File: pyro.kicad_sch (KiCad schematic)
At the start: 6 parts, among them J14 PYRO, Q1 CSD17571Q2

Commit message: replaced signal blocks, shortening board, adding precise positioning
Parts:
- renumbered J14 to J15, Q1 to Q2, R51 to R52, R52 to R53, R53 to R54
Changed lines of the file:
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@@
 		(dnp no)
 		(fields_autoplaced yes)
-		(property "Reference" "#PWR0108"
+		(property "Reference" "#PWR0113"
 			(at 123.19 80.01 0)
 			(hide yes)
@@
 			(project "mixed_signal_sensor_board"
 				(path "/5c142d60-6b5a-463f-88b9-a177eae7f51b/4774a8d6-944e-4a86-81b4-a8db3fe171f5"
-					(reference "#PWR0117")
-					(unit 1)
-				)
-				(path "/5c142d60-6b5a-463f-88b9-a177eae7f51b/5edb0f01-38b3-4437-8c04-080f84fffaff"
-					(reference "#PWR0108")
-					(unit 1)
-				)
-				(path "/5c142d60-6b5a-463f-88b9-a177eae7f51b/c1d5fa9f-2091-4637-b914-ef00b6553b9c"
-					(reference "#PWR0111")
-					(unit 1)
-				)
-				(path "/5c142d60-6b5a-463f-88b9-a177eae7f51b/d9a7688a-1f4c-4937-a470-cef945448846"
-					(reference "#PWR0114")
+					(reference "#PWR0122")
+					(unit 1)
+				)
+				(path "/5c142d60-6b5a-463f-88b9-a177eae7f51b/5edb0f01-38b3-4437-8c04-080f84fffaff"
+					(reference "#PWR0113")
+					(unit 1)
+				)
+				(path "/5c142d60-6b5a-463f-88b9-a177eae7f51b/c1d5fa9f-2091-4637-b914-ef00b6553b9c"
+					(reference "#PWR0116")
+					(unit 1)
+				)
+				(path "/5c142d60-6b5a-463f-88b9-a177eae7f51b/d9a7688a-1f4c-4937-a470-cef945448846"
+					(reference "#PWR0119")
 					(unit 1)
 				)
@@
 		(dnp no)
 		(fields_autoplaced yes)
-		(property "Reference" "#PWR0110"
+		(property "Reference" "#PWR0115"
 			(at 135.89 74.93 0)
 			(hide yes)
@@
 			(project "mixed_signal_sensor_board"
 				(path "/5c142d60-6b5a-463f-88b9-a177eae7f51b/4774a8d6-944e-4a86-81b4-a8db3fe171f5"
-					(reference "#PWR0119")
-					(unit 1)
-				)
-				(path "/5c142d60-6b5a-463f-88b9-a177eae7f51b/5edb0f01-38b3-4437-8c04-080f84fffaff"
-					(reference "#PWR0110")
-					(unit 1)
-				)
-				(path "/5c142d60-6b5a-463f-88b9-a177eae7f51b/c1d5fa9f-2091-4637-b914-ef00b6553b9c"
-					(reference "#PWR0113")
-					(unit 1)
-				)
-				(path "/5c142d60-6b5a-463f-88b9-a177eae7f51b/d9a7688a-1f4c-4937-a470-cef945448846"
-					(reference "#PWR0116")
+					(reference "#PWR0124")
+					(unit 1)
+				)
+				(path "/5c142d60-6b5a-463f-88b9-a177eae7f51b/5edb0f01-38b3-4437-8c04-080f84fffaff"
+					(reference "#PWR0115")
+					(unit 1)
+				)
+				(path "/5c142d60-6b5a-463f-88b9-a177eae7f51b/c1d5fa9f-2091-4637-b914-ef00b6553b9c"
+					(reference "#PWR0118")
+					(unit 1)
+				)
+				(path "/5c142d60-6b5a-463f-88b9-a177eae7f51b/d9a7688a-1f4c-4937-a470-cef945448846"
+					(reference "#PWR0121")
 					(unit 1)
 				)
@@
 		(in_pos_files yes)
 		(dnp no)
-		(property "Reference" "R51"
+		(property "Reference" "R52"
 			(at 111.506 101.854 0)
 			(show_name no)
@@
 			(project "mixed_signal_sensor_board"
 				(path "/5c142d60-6b5a-463f-88b9-a177eae7f51b/4774a8d6-944e-4a86-81b4-a8db3fe171f5"
-					(reference "R60")
-					(unit 1)
-				)
-				(path "/5c142d60-6b5a-463f-88b9-a177eae7f51b/5edb0f01-38b3-4437-8c04-080f84fffaff"
-					(reference "R51")
-					(unit 1)
-				)
-				(path "/5c142d60-6b5a-463f-88b9-a177eae7f51b/c1d5fa9f-2091-4637-b914-ef00b6553b9c"
-					(reference "R54")
-					(unit 1)
-				)
-				(path "/5c142d60-6b5a-463f-88b9-a177eae7f51b/d9a7688a-1f4c-4937-a470-cef945448846"
-					(reference "R57")
+					(reference "R61")
+					(unit 1)
+				)
+				(path "/5c142d60-6b5a-463f-88b9-a177eae7f51b/5edb0f01-38b3-4437-8c04-080f84fffaff"
+					(reference "R52")
+					(unit 1)
+				)
+				(path "/5c142d60-6b5a-463f-88b9-a177eae7f51b/c1d5fa9f-2091-4637-b914-ef00b6553b9c"
+					(reference "R55")
+					(unit 1)
+				)
+				(path "/5c142d60-6b5a-463f-88b9-a177eae7f51b/d9a7688a-1f4c-4937-a470-cef945448846"
+					(reference "R58")
 					(unit 1)
 				)
@@
 		(in_pos_files yes)
 		(dnp no)
-		(property "Reference" "R53"
+		(property "Reference" "R54"
 			(at 139.954 84.074 0)
 			(show_name no)
@@
 			(project "mixed_signal_sensor_board"
 				(path "/5c142d60-6b5a-463f-88b9-a177eae7f51b/4774a8d6-944e-4a86-81b4-a8db3fe171f5"
-					(reference "R62")
-					(unit 1)
-				)
-				(path "/5c142d60-6b5a-463f-88b9-a177eae7f51b/5edb0f01-38b3-4437-8c04-080f84fffaff"
-					(reference "R53")
-					(unit 1)
-				)
-				(path "/5c142d60-6b5a-463f-88b9-a177eae7f51b/c1d5fa9f-2091-4637-b914-ef00b6553b9c"
-					(reference "R56")
-					(unit 1)
-				)
-				(path "/5c142d60-6b5a-463f-88b9-a177eae7f51b/d9a7688a-1f4c-4937-a470-cef945448846"
-					(reference "R59")
+					(reference "R63")
+					(unit 1)
+				)
+				(path "/5c142d60-6b5a-463f-88b9-a177eae7f51b/5edb0f01-38b3-4437-8c04-080f84fffaff"
+					(reference "R54")
+					(unit 1)
+				)
+				(path "/5c142d60-6b5a-463f-88b9-a177eae7f51b/c1d5fa9f-2091-4637-b914-ef00b6553b9c"
+					(reference "R57")
+					(unit 1)
+				)
+				(path "/5c142d60-6b5a-463f-88b9-a177eae7f51b/d9a7688a-1f4c-4937-a470-cef945448846"
+					(reference "R60")
 					(unit 1)
 				)
@@
 		(in_pos_files yes)
 		(dnp no)
-		(property "Reference" "R52"
+		(property "Reference" "R53"
 			(at 129.54 86.614 90)
 			(show_name no)
@@
 			(project "mixed_signal_sensor_board"
 				(path "/5c142d60-6b5a-463f-88b9-a177eae7f51b/4774a8d6-944e-4a86-81b4-a8db3fe171f5"
-					(reference "R61")
-					(unit 1)
-				)
-				(path "/5c142d60-6b5a-463f-88b9-a177eae7f51b/5edb0f01-38b3-4437-8c04-080f84fffaff"
-					(reference "R52")
-					(unit 1)
-				)
-				(path "/5c142d60-6b5a-463f-88b9-a177eae7f51b/c1d5fa9f-2091-4637-b914-ef00b6553b9c"
-					(reference "R55")
-					(unit 1)
-				)
-				(path "/5c142d60-6b5a-463f-88b9-a177eae7f51b/d9a7688a-1f4c-4937-a470-cef945448846"
-					(reference "R58")
+					(reference "R62")
+					(unit 1)
+				)
+				(path "/5c142d60-6b5a-463f-88b9-a177eae7f51b/5edb0f01-38b3-4437-8c04-080f84fffaff"
+					(reference "R53")
+					(unit 1)
+				)
+				(path "/5c142d60-6b5a-463f-88b9-a177eae7f51b/c1d5fa9f-2091-4637-b914-ef00b6553b9c"
+					(reference "R56")
+					(unit 1)
+				)
+				(path "/5c142d60-6b5a-463f-88b9-a177eae7f51b/d9a7688a-1f4c-4937-a470-cef945448846"
+					(reference "R59")
 					(unit 1)
 				)
@@
 		(dnp no)
 		(fields_autoplaced yes)
-		(property "Reference" "Q1"
+		(property "Reference" "Q2"
 			(at 127 97.7899 0)
 			(show_name no)
@@
 			(project "mixed_signal_sensor_board"
 				(path "/5c142d60-6b5a-463f-88b9-a177eae7f51b/4774a8d6-944e-4a86-81b4-a8db3fe171f5"
+					(reference "Q5")
+					(unit 1)
+				)
+				(path "/5c142d60-6b5a-463f-88b9-a177eae7f51b/5edb0f01-38b3-4437-8c04-080f84fffaff"
+					(reference "Q2")
+					(unit 1)
+				)
+				(path "/5c142d60-6b5a-463f-88b9-a177eae7f51b/c1d5fa9f-2091-4637-b914-ef00b6553b9c"
+					(reference "Q3")
+					(unit 1)
+				)
+				(path "/5c142d60-6b5a-463f-88b9-a177eae7f51b/d9a7688a-1f4c-4937-a470-cef945448846"
 					(reference "Q4")
-					(unit 1)
-				)
-				(path "/5c142d60-6b5a-463f-88b9-a177eae7f51b/5edb0f01-38b3-4437-8c04-080f84fffaff"
-					(reference "Q1")
-					(unit 1)
-				)
-				(path "/5c142d60-6b5a-463f-88b9-a177eae7f51b/c1d5fa9f-2091-4637-b914-ef00b6553b9c"
-					(reference "Q2")
-					(unit 1)
-				)
-				(path "/5c142d60-6b5a-463f-88b9-a177eae7f51b/d9a7688a-1f4c-4937-a470-cef945448846"
-					(reference "Q3")
 					(unit 1)
 				)
@@
 		(dnp no)
 		(fields_autoplaced yes)
-		(property "Reference" "#PWR0109"
+		(property "Reference" "#PWR0114"
 			(at 123.19 113.03 0)
 			(hide yes)
@@
 			(project "mixed_signal_sensor_board"
 				(path "/5c142d60-6b5a-463f-88b9-a177eae7f51b/4774a8d6-944e-4a86-81b4-a8db3fe171f5"
-					(reference "#PWR0118")
-					(unit 1)
-				)
-				(path "/5c142d60-6b5a-463f-88b9-a177eae7f51b/5edb0f01-38b3-4437-8c04-080f84fffaff"
-					(reference "#PWR0109")
-					(unit 1)
-				)
-				(path "/5c142d60-6b5a-463f-88b9-a177eae7f51b/c1d5fa9f-2091-4637-b914-ef00b6553b9c"
-					(reference "#PWR0112")
-					(unit 1)
-				)
-				(path "/5c142d60-6b5a-463f-88b9-a177eae7f51b/d9a7688a-1f4c-4937-a470-cef945448846"
-					(reference "#PWR0115")
+					(reference "#PWR0123")
+					(unit 1)
+				)
+				(path "/5c142d60-6b5a-463f-88b9-a177eae7f51b/5edb0f01-38b3-4437-8c04-080f84fffaff"
+					(reference "#PWR0114")
+					(unit 1)
+				)
+				(path "/5c142d60-6b5a-463f-88b9-a177eae7f51b/c1d5fa9f-2091-4637-b914-ef00b6553b9c"
+					(reference "#PWR0117")
+					(unit 1)
+				)
+				(path "/5c142d60-6b5a-463f-88b9-a177eae7f51b/d9a7688a-1f4c-4937-a470-cef945448846"
+					(reference "#PWR0120")
 					(unit 1)
 				)
@@
 		(in_pos_files yes)
 		(dnp no)
-		(property "Reference" "J14"
+		(property "Reference" "J15"
 			(at 113.538 86.36 0)
 			(show_name no)
@@
 			(project "mixed_signal_sensor_board"
 				(path "/5c142d60-6b5a-463f-88b9-a177eae7f51b/4774a8d6-944e-4a86-81b4-a8db3fe171f5"
+					(reference "J18")
+					(unit 1)
+				)
+				(path "/5c142d60-6b5a-463f-88b9-a177eae7f51b/5edb0f01-38b3-4437-8c04-080f84fffaff"
+					(reference "J15")
+					(unit 1)
+				)
+				(path "/5c142d60-6b5a-463f-88b9-a177eae7f51b/c1d5fa9f-2091-4637-b914-ef00b6553b9c"
+					(reference "J16")
+					(unit 1)
+				)
+				(path "/5c142d60-6b5a-463f-88b9-a177eae7f51b/d9a7688a-1f4c-4937-a470-cef945448846"
 					(reference "J17")
 					(unit 1)
 				)
-				(path "/5c142d60-6b5a-463f-88b9-a177eae7f51b/5edb0f01-38b3-4437-8c04-080f84fffaff"
-					(reference "J14")
-					(unit 1)
-				)
-				(path "/5c142d60-6b5a-463f-88b9-a177eae7f51b/c1d5fa9f-2091-4637-b914-ef00b6553b9c"
-					(reference "J15")
-					(unit 1)
-				)
-				(path "/5c142d60-6b5a-463f-88b9-a177eae7f51b/d9a7688a-1f4c-4937-a470-cef945448846"
-					(reference "J16")
-					(unit 1)
-				)

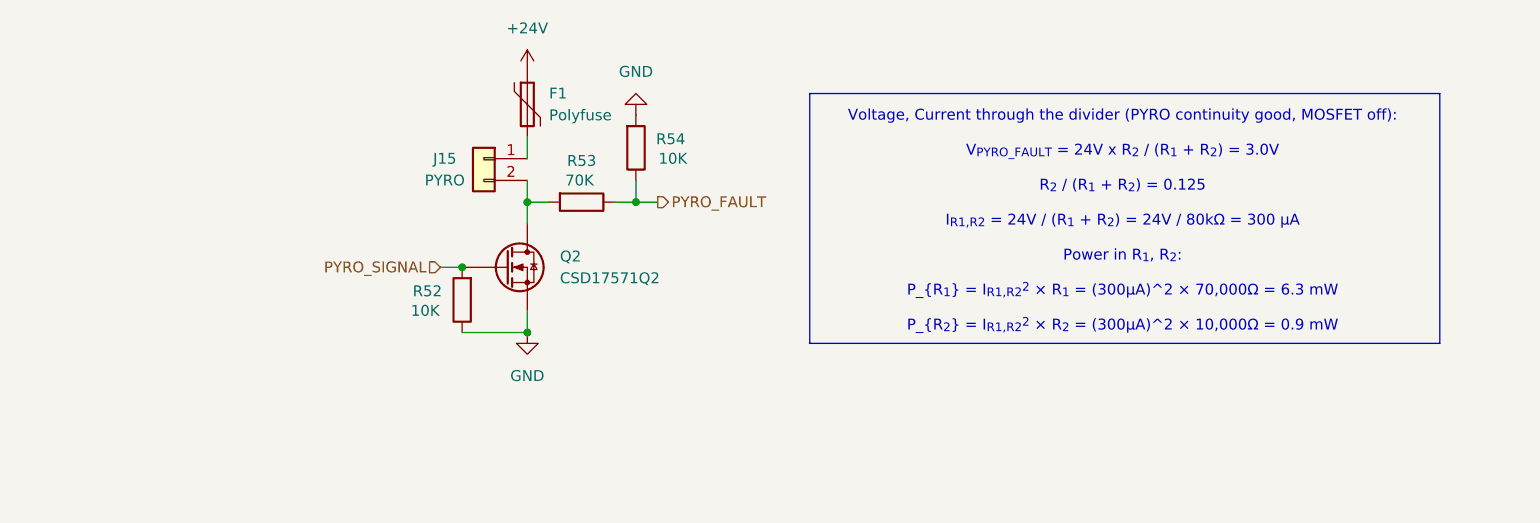
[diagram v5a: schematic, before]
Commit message: removed SPI, I2C, compacting pyro channels, new pyro schematic
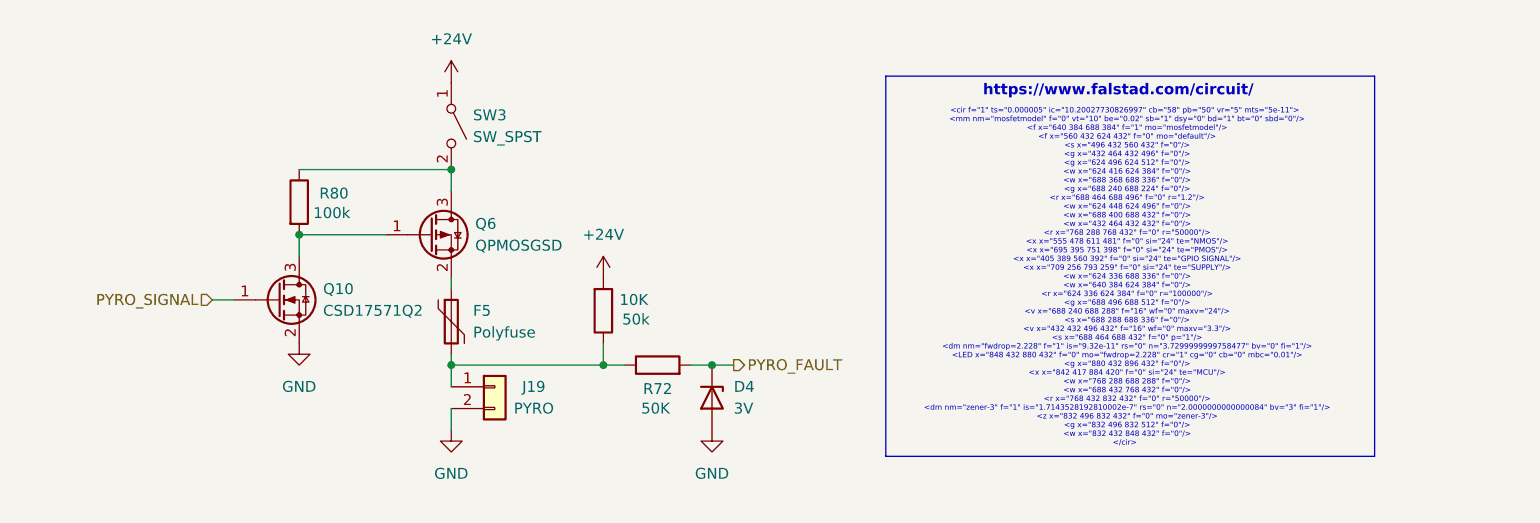
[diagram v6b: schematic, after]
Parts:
- removed F1: Polyfuse, Fuse:Fuse_1210_3225Metric, symbol Device:Polyfuse
- removed J15: PYRO, Connector_JST:JST_PH_S2B-PH-SM4-TB_1x02-1MP_P2.00mm_Horizontal, symbol Connector_Generic:Conn_01x02
- removed Q2: CSD17571Q2, CSD17571Q2:CSD17571Q2, symbol Device:Q_NMOS
- removed R52, R54: 10K, Resistor_SMD:R_0402_1005Metric, symbol Device:R
- removed R53: 70K, Resistor_SMD:R_0402_1005Metric, symbol Device:R
- added 50k: 10K, Resistor_SMD:R_0402_1005Metric, symbol Device:R
- added D4: 3V, symbol Device:D_Zener
- added F5: Polyfuse, Fuse:Fuse_1210_3225Metric, symbol Device:Polyfuse
- added J19: PYRO, Connector_JST:JST_PH_S2B-PH-SM4-TB_1x02-1MP_P2.00mm_Horizontal, symbol Connector_Generic:Conn_01x02
- added Q10: CSD17571Q2, CSD17571Q2:CSD17571Q2, symbol Transistor_FET:Q_NMOS_GSD
- added Q6: QPMOSGSD, symbol Transistor_FET:Q_PMOS_GSD
- added R72: 50K, Resistor_SMD:R_0402_1005Metric, symbol Device:R
- added R80: 100k, Resistor_SMD:R_0402_1005Metric, symbol Device:R
- added SW3: SW_SPST, symbol Switch:SW_SPST
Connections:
- net +24V: now also 50k.2, SW3.1 (A)
- net GND: now also D4.2 (A), J19.2 (Pin_2), Q10.2 (S)
- net PYRO_FAULT: now also D4.1 (K), R72.2
- net PYRO_SIGNAL: now also Q10.1 (G)
- new net: Q10.3 (D), Q6.1 (G), R80.2
- new net: F5.1, Q6.2 (S)
- new net: 50k.1, F5.2, J19.1 (Pin_1), R72.1
- new net: Q6.3 (D), R80.1, SW3.2 (B)
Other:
- note added: "<cir f="1" ts="0.000005" ic="10.20027730826997" cb="58" pb="50" vr="5" mts="5e-11"> <mm nm="mosfetmodel" f="0" vt="10" be="0.02" sb="1" dsy="0" bd="1" bt="0" sbd="0"/> <f x="640 384 688 384" f="1" mo="mosfetmodel"/> <f x="560 432 624 432" f="0" mo="default"/> <s x="496 432 560 432" f="0"/> <g x="432 464 432 496" f="0"/> <g x="624 496 624 512" f="0"/> <w x="624 416 624 384" f="0"/> <w x="688 368 6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"
- note added: "https://www.falstad.com/circuit/"
- note removed: "Voltage, Current through the divider (PYRO continuity good, MOSFET off): V_{PYRO_FAULT} = 24V x R_{2} / (R_{1} + R_{2}) = 3.0V R_{2} / (R_{1} + R_{2}) = 0.125 I_{R1,R2} = 24V / (R_{1} + R_{2}) = 24V / 80kΩ = 300 µA Power in R_{1}, R_{2}: P_{R_{1}} = I_{R1,R2}^{2} × R_{1} = (300µA)^2 × 70,000Ω = 6.3 mW P_{R_{2}} = I_{R1,R2}^{2} × R_{2} = (300µA)^2 × 10,000Ω = 0.9 mW"

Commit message: New pyro layout, SWDIO, SWCLK, USART2 TX RX, 70x50mm board
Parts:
- removed Q6: QPMOSGSD, symbol Transistor_FET:Q_PMOS_GSD
- removed SW3: SW_SPST, symbol Switch:SW_SPST
- added Q2: IRLML5103TRPBF, Package_TO_SOT_SMD:SOT-23, symbol Transistor_FET:Q_PMOS_GSD
- renumbered 50k to 50k1
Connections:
- net at Q10.3 (D), R80.2: now also Q2.1 (G)
- net at F5.1: now also Q2.2 (S)
- net ARM: now reaches R80.1
- net ARM: now also Q2.3 (D)
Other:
- note added: "<cir f="1" ts="0.000005" ic="10.20027730826997" cb="58" pb="50" vr="5" mts="5e-11"> <mm nm="mosfetmodel" f="0" vt="10" be="0.02" sb="1" dsy="0" bd="1" bt="0" sbd="0"/> <f x="640 384 688 384" f="1" mo="mosfetmodel"/> <f x="560 432 624 432" f="0" mo="default"/> <s x="496 432 560 432" f="0" p="1"/> <g x="432 464 432 496" f="0"/> <g x="624 496 624 512" f="0"/> <w x="624 416 624 384" f="0"/> <w x="688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"
- note removed: "<cir f="1" ts="0.000005" ic="10.20027730826997" cb="58" pb="50" vr="5" mts="5e-11"> <mm nm="mosfetmodel" f="0" vt="10" be="0.02" sb="1" dsy="0" bd="1" bt="0" sbd="0"/> <f x="640 384 688 384" f="1" mo="mosfetmodel"/> <f x="560 432 624 432" f="0" mo="default"/> <s x="496 432 560 432" f="0"/> <g x="432 464 432 496" f="0"/> <g x="624 496 624 512" f="0"/> <w x="624 416 624 384" f="0"/> <w x="688 368 6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"
- moved on the sheet: 50k1, D4, R72

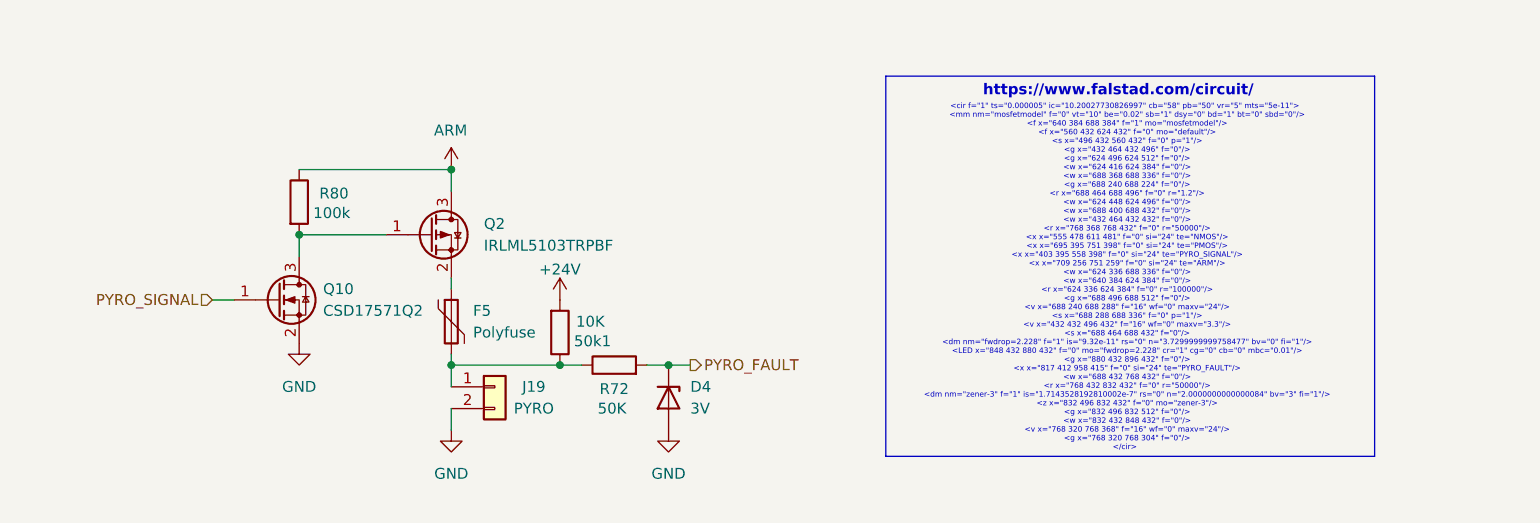
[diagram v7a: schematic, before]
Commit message: PYRO done, schematic structure/convention update, pyro and reverse polarity components selected
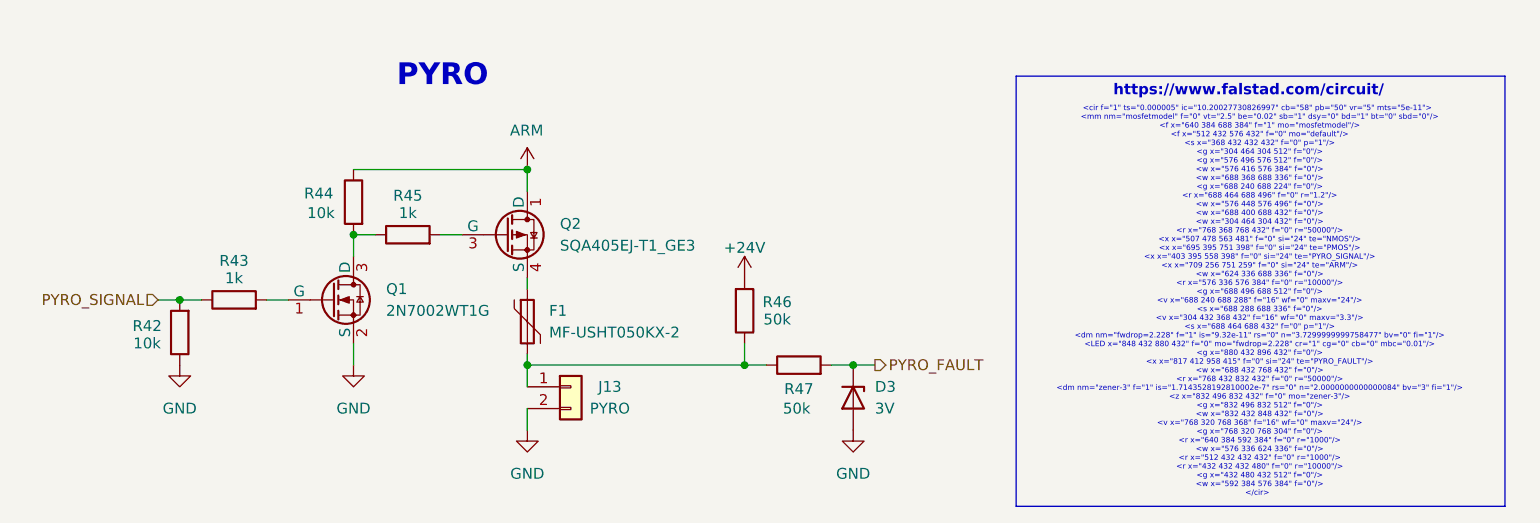
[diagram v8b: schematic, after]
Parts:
- removed Q10: CSD17571Q2, CSD17571Q2:CSD17571Q2, symbol Transistor_FET:Q_NMOS_GSD
- added Q1: 2N7002WT1G, Package_TO_SOT_SMD:SOT-323_SC-70, symbol Transistor_FET:Q_NMOS_GSD
- added R42: 10k, Resistor_SMD:R_0402_1005Metric, symbol Device:R
- added R43, R45: 1k, Resistor_SMD:R_0402_1005Metric, symbol Device:R
- F1: renamed from F5; value Polyfuse -> MF-USHT050KX-2
- Q2: value IRLML5103TRPBF -> SQA405EJ-T1_GE3; footprint Package_TO_SOT_SMD:SOT-23 -> Package_TO_SOT_SMD:Vishay_PowerPAK_SC70-6L_Single
- R44: renamed from R80; value 100k -> 10k
- R46: renamed from 50k1; value 10K -> 50k
- R47: renamed from R72; value 50K -> 50k
- renumbered D4 to D3, J19 to J13
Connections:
- net ARM: now also Q2.1 (D); no longer Q2.3 (D)
- net GND: now also Q1.2 (S), R42.1
- net PYRO_SIGNAL: now also R42.2, R43.1
- net at R44.2: now also Q1.3 (D), R45.1; no longer Q2.1 (G)
- net at F1.1: now also Q2.4 (S); no longer Q2.2 (S)
- new net: Q1.1 (G), R43.2
- new net: Q2.3 (G), R45.2
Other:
- note added: "<cir f="1" ts="0.000005" ic="10.20027730826997" cb="58" pb="50" vr="5" mts="5e-11"> <mm nm="mosfetmodel" f="0" vt="2.5" be="0.02" sb="1" dsy="0" bd="1" bt="0" sbd="0"/> <f x="640 384 688 384" f="1" mo="mosfetmodel"/> <f x="512 432 576 432" f="0" mo="default"/> <s x="368 432 432 432" f="0" p="1"/> <g x="304 464 304 512" f="0"/> <g x="576 496 576 512" f="0"/> <w x="576 416 576 384" f="0"/> <w x="68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"
- note added: "PYRO"
- note removed: "<cir f="1" ts="0.000005" ic="10.20027730826997" cb="58" pb="50" vr="5" mts="5e-11"> <mm nm="mosfetmodel" f="0" vt="10" be="0.02" sb="1" dsy="0" bd="1" bt="0" sbd="0"/> <f x="640 384 688 384" f="1" mo="mosfetmodel"/> <f x="560 432 624 432" f="0" mo="default"/> <s x="496 432 560 432" f="0" p="1"/> <g x="432 464 432 496" f="0"/> <g x="624 496 624 512" f="0"/> <w x="624 416 624 384" f="0"/> <w x="688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"
- moved on the sheet: D3, F1, J13, R44, R46, R47
